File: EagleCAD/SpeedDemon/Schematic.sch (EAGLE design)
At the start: 69 parts, among them Q1 DMC2700, U3 LM3676, U4 STM32F072-LQFP48

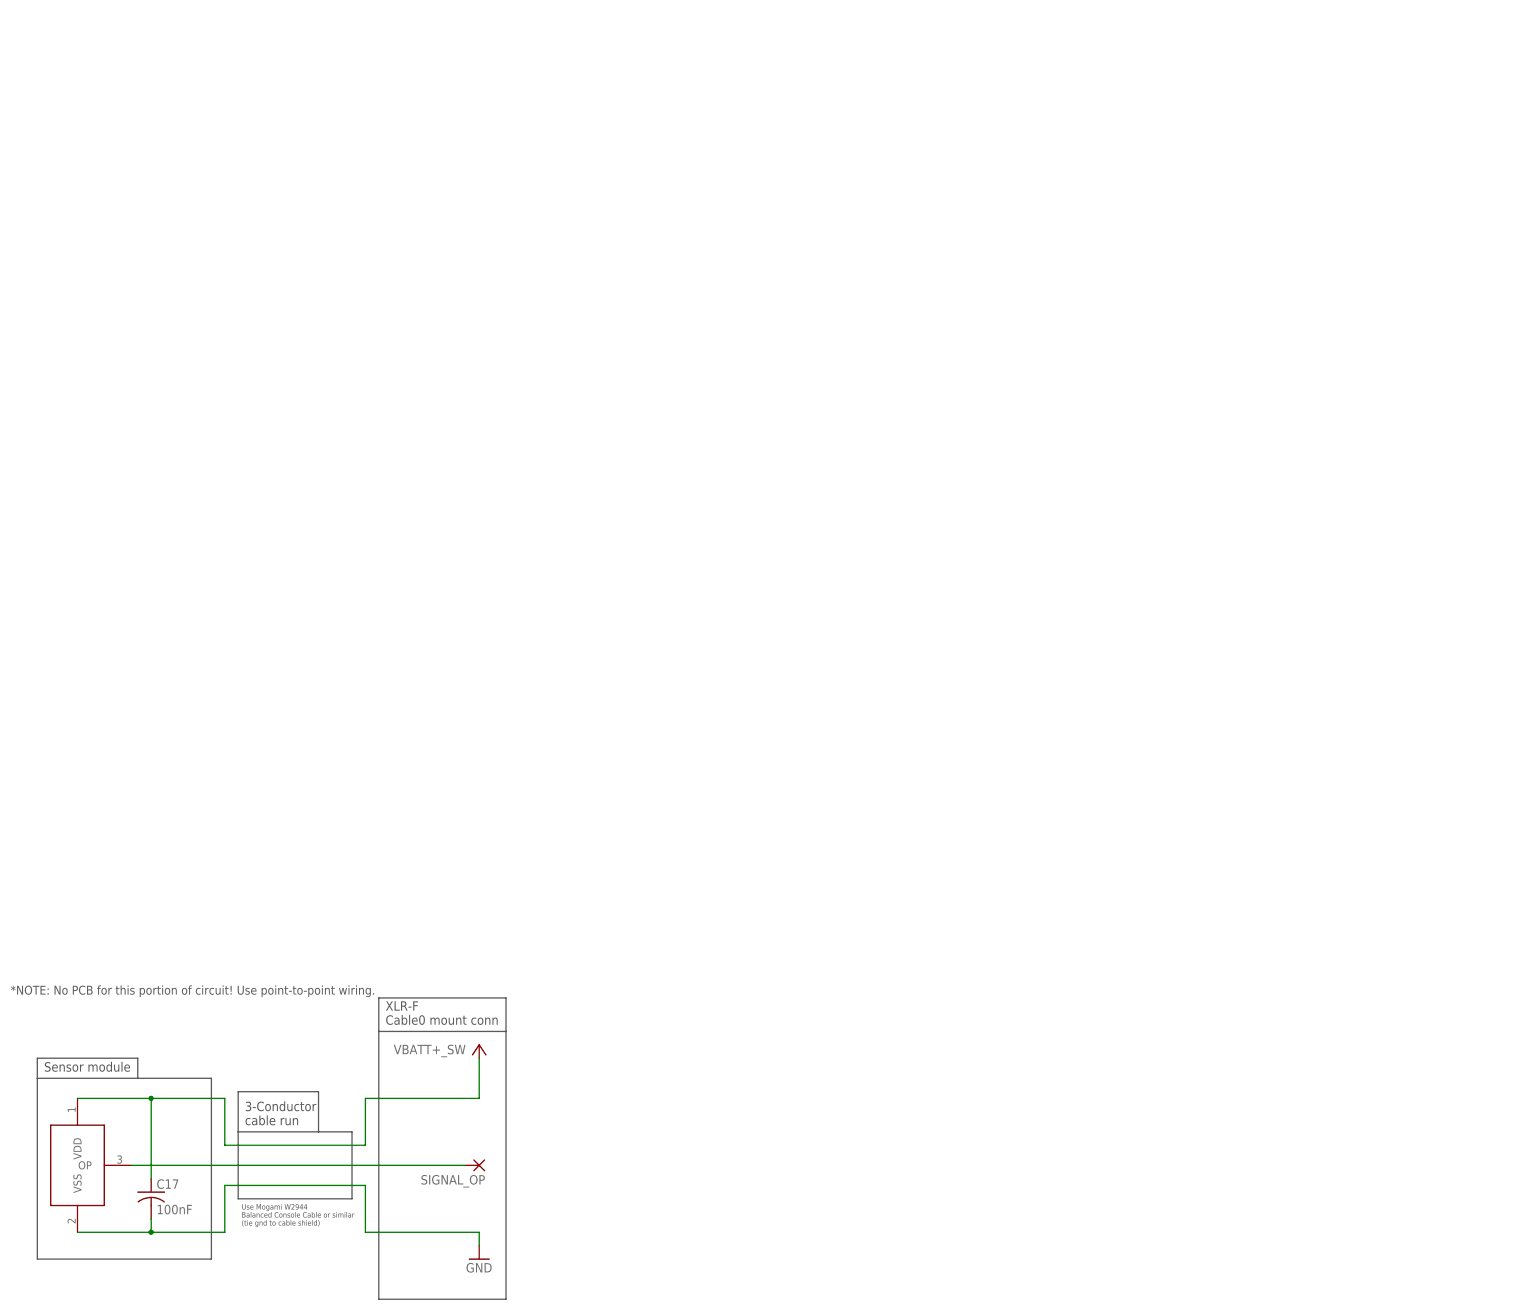
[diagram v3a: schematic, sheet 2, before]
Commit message: Fixed frame of second page
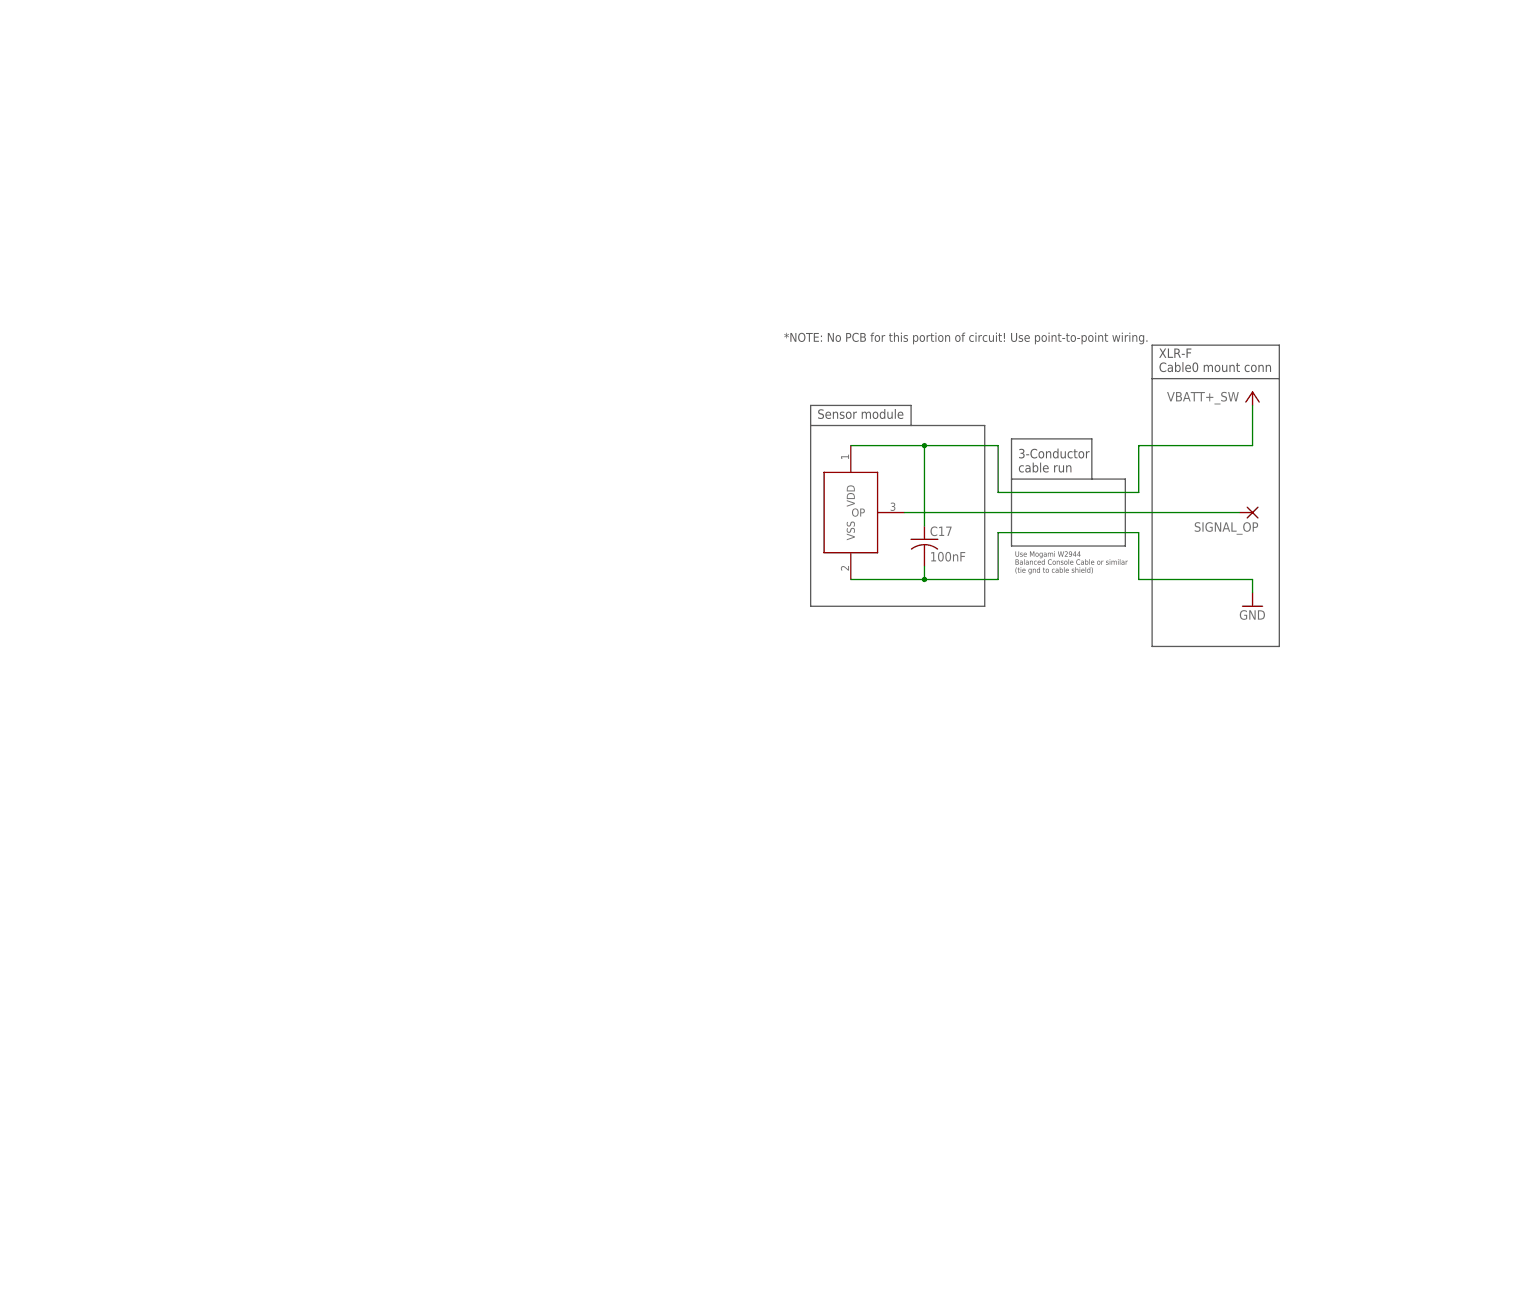
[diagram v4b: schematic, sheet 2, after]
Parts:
- removed R5: 22, rcl:R-US_R0805
- removed U5: (no value), US5881:US5881
- added U1A: (no value), US5881:US5881
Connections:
- removed net N$5: JP1.2, R5.2
- net FL_SWCLK: now also JP1.2; no longer R5.1
- net GND: now also U1A.VSS; no longer U5.VSS
- net N$37: now also U1A.OP; no longer U5.OP
- net VBATT+_SW: now also U1A.VDD; no longer U5.VDD
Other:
- moved on the sheet: C17, SIGNAL_OP

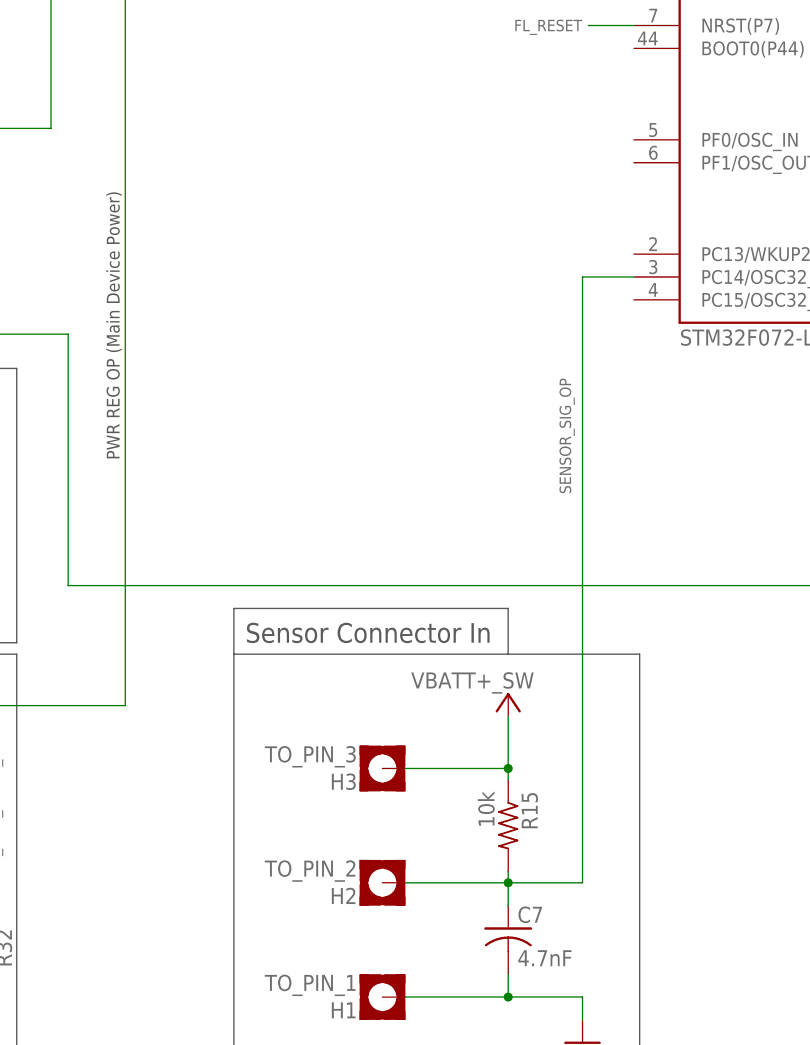
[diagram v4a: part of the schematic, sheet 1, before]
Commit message: added external OSC circuit to schematic, several datasheets
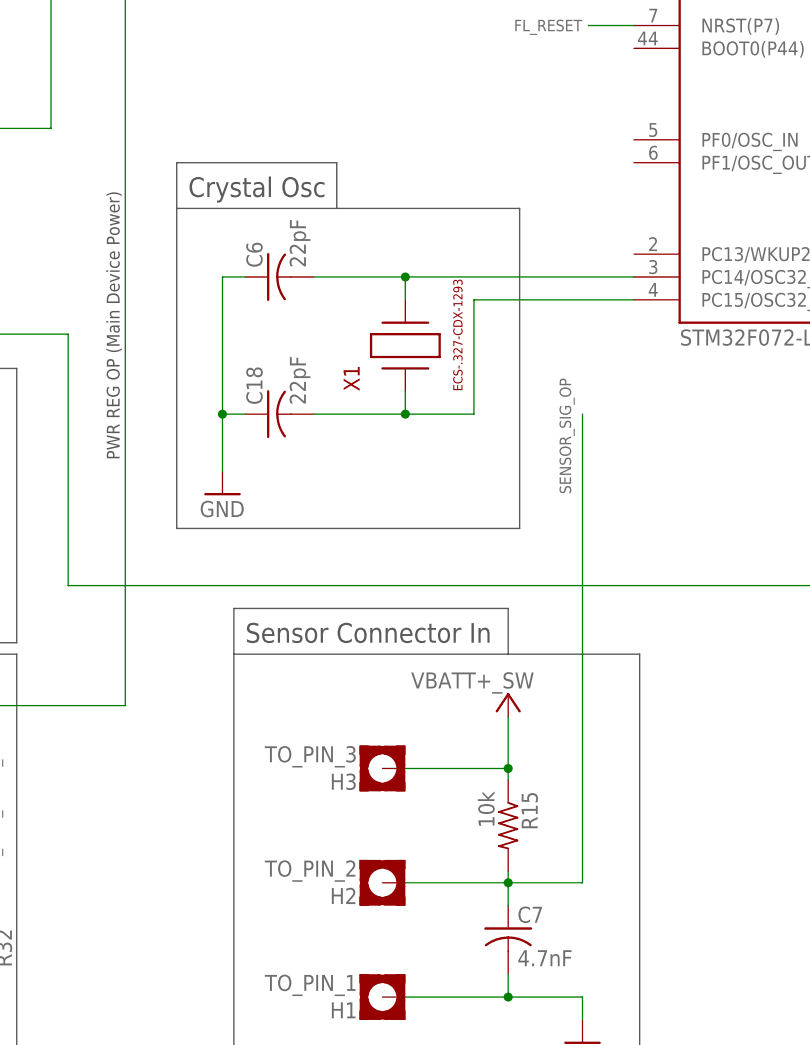
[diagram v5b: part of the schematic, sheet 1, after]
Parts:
- added C18, C6: 22pF, LCRD_SMD_generics:C_0805_NP
- added X1: (no value), LCRD_SMD_generics:XC2292CT-ND
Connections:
- new net N$11: C18.2, U4.PC15/OSC32_OUT, X1.2
- new net N$5: C6.2, U4.PC14/OSC32_IN, X1.1
- net GND: now also C18.1, C6.1
- net SENSOR_SIG_OP: no longer U4.PC14/OSC32_IN
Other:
- note added: "Crystal Osc"
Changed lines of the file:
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@@
 <setting verticaltext="up"/>
 </settings>
-<grid distance="0.025" unitdist="inch" unit="inch" style="lines" multiple="1" display="yes" altdistance="0.01" altunitdist="inch" altunit="inch"/>
+<grid distance="0.05" unitdist="inch" unit="inch" style="lines" multiple="1" display="no" altdistance="0.01" altunitdist="inch" altunit="inch"/>
 <layers>
 <layer number="1" name="Top" color="4" fill="1" visible="no" active="no"/>
@@
 <part name="U1A" library="US5881" deviceset="US5881" device=""/>
 <part name="FRAME2" library="frames" library_urn="urn:adsk.eagle:library:229" deviceset="A3L-LOC" device=""/>
+<part name="X1" library="LCRD_SMD_generics" deviceset="XC2292CT-ND" device=""/>
+<part name="C6" library="LCRD_SMD_generics" deviceset="C_0805_NP" device="" value="22pF"/>
+<part name="C18" library="LCRD_SMD_generics" deviceset="C_0805_NP" device="" value="22pF"/>
+<part name="GND8" library="supply1" library_urn="urn:adsk.eagle:library:371" deviceset="GND" device=""/>
 </parts>
 <sheets>
@@
 <text x="344.17" y="20.32" size="2.1844" layer="97">Main PCB</text>
 <text x="119.38" y="5.715" size="1.27" layer="97">See p. 2 for sensor module schematic</text>
+<wire x1="111.76" y1="71.12" x2="149.86" y2="71.12" width="0.1524" layer="97"/>
+<wire x1="149.86" y1="71.12" x2="149.86" y2="106.68" width="0.1524" layer="97"/>
+<wire x1="149.86" y1="106.68" x2="129.54" y2="106.68" width="0.1524" layer="97"/>
+<wire x1="129.54" y1="106.68" x2="111.76" y2="106.68" width="0.1524" layer="97"/>
+<wire x1="111.76" y1="106.68" x2="111.76" y2="71.12" width="0.1524" layer="97"/>
+<text x="113.03" y="107.95" size="2.1844" layer="97">Crystal Osc</text>
+<wire x1="111.76" y1="106.68" x2="111.76" y2="111.76" width="0.1524" layer="97"/>
+<wire x1="111.76" y1="111.76" x2="129.54" y2="111.76" width="0.1524" layer="97"/>
+<wire x1="129.54" y1="111.76" x2="129.54" y2="106.68" width="0.1524" layer="97"/>
 </plain>
 <instances>
@@
 <instance part="R32" gate="G$1" x="90.17" y="22.86" rot="R270"/>
 <instance part="GND22" gate="1" x="90.17" y="12.065"/>
+<instance part="X1" gate="G$1" x="137.16" y="91.44" rot="R90"/>
+<instance part="C6" gate="G$1" x="121.92" y="99.06" rot="R90"/>
+<instance part="C18" gate="G$1" x="121.92" y="83.82" rot="R90"/>
+<instance part="GND8" gate="1" x="116.84" y="74.93"/>
 </instances>
 <busses>
@@
 <pinref part="GND22" gate="1" pin="GND"/>
 <wire x1="90.17" y1="17.78" x2="90.17" y2="14.605" width="0.1524" layer="91"/>
+</segment>
+<segment>
+<pinref part="C18" gate="G$1" pin="1"/>
+<wire x1="119.38" y1="83.82" x2="116.84" y2="83.82" width="0.1524" layer="91"/>
+<wire x1="116.84" y1="83.82" x2="116.84" y2="99.06" width="0.1524" layer="91"/>
+<pinref part="C6" gate="G$1" pin="1"/>
+<wire x1="116.84" y1="99.06" x2="119.38" y2="99.06" width="0.1524" layer="91"/>
+<pinref part="GND8" gate="1" pin="GND"/>
+<wire x1="116.84" y1="83.82" x2="116.84" y2="77.47" width="0.1524" layer="91"/>
+<junction x="116.84" y="83.82"/>
 </segment>
 </net>
@@
 <wire x1="148.59" y1="31.75" x2="156.845" y2="31.75" width="0.1524" layer="91"/>
 <label x="155.575" y="74.93" size="1.27" layer="95" rot="R90"/>
-<wire x1="156.845" y1="31.75" x2="156.845" y2="99.06" width="0.1524" layer="91"/>
-<pinref part="U4" gate="G$1" pin="PC14/OSC32_IN"/>
-<wire x1="156.845" y1="99.06" x2="162.56" y2="99.06" width="0.1524" layer="91"/>
+<wire x1="156.845" y1="31.75" x2="156.845" y2="83.82" width="0.1524" layer="91"/>
 </segment>
 </net>
@@
 </segment>
 </net>
+<net name="N$11" class="0">
+<segment>
+<pinref part="U4" gate="G$1" pin="PC15/OSC32_OUT"/>
+<wire x1="162.56" y1="96.52" x2="144.78" y2="96.52" width="0.1524" layer="91"/>
+<wire x1="144.78" y1="96.52" x2="144.78" y2="83.82" width="0.1524" layer="91"/>
+<wire x1="144.78" y1="83.82" x2="137.16" y2="83.82" width="0.1524" layer="91"/>
+<pinref part="X1" gate="G$1" pin="2"/>
+<wire x1="137.16" y1="83.82" x2="137.16" y2="86.36" width="0.1524" layer="91"/>
+<pinref part="C18" gate="G$1" pin="2"/>
+<wire x1="137.16" y1="83.82" x2="127" y2="83.82" width="0.1524" layer="91"/>
+<junction x="137.16" y="83.82"/>
+</segment>
+</net>
+<net name="N$5" class="0">
+<segment>
+<pinref part="U4" gate="G$1" pin="PC14/OSC32_IN"/>
+<wire x1="162.56" y1="99.06" x2="137.16" y2="99.06" width="0.1524" layer="91"/>
+<pinref part="X1" gate="G$1" pin="1"/>
+<wire x1="137.16" y1="99.06" x2="137.16" y2="96.52" width="0.1524" layer="91"/>
+<pinref part="C6" gate="G$1" pin="2"/>
+<wire x1="137.16" y1="99.06" x2="127" y2="99.06" width="0.1524" layer="91"/>
+<junction x="137.16" y="99.06"/>
+</segment>
+</net>
